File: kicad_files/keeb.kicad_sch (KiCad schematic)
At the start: 169 parts, among them SW1 SW_Push, SW10 SW_Push, SW11 SW_Push, SW12 SW_Push, SW13 SW_Push, SW14 SW_Push, SW15 SW_Push, SW16 SW_Push, SW17 SW_Push, SW18 SW_Push, SW19 SW_Push, SW2 SW_Push, SW20 SW_Push, SW21 SW_Push, SW22 SW_Push, SW23 SW_Push, SW24 SW_Push, SW25 SW_Push, SW26 SW_Push, SW27 SW_Push, SW28 SW_Push, SW29 SW_Push, SW3 SW_Push, SW30 SW_Push, SW31 SW_Push, SW32 SW_Push, SW33 SW_Push, SW34 SW_Push, SW35 SW_Push, SW36 SW_Push, SW37 SW_Push, SW38 SW_Push, SW39 SW_Push, SW4 SW_Push, SW40 SW_Push, SW41 SW_Push, SW42 SW_Push, SW43 SW_Push, SW44 SW_Push, SW45 SW_Push, SW46 SW_Push, SW47 SW_Push, SW48 SW_Push, SW49 SW_Push, SW5 SW_Push, SW50 SW_Push, SW51 SW_Push, SW52 SW_Push, SW53 SW_Push, SW54 SW_Push, SW55 SW_Push, SW56 SW_Push, SW57 SW_Push, SW58 SW_Push, SW59 SW_Push, SW6 SW_Push, SW60 SW_Push, SW61 SW_Push, SW62 SW_Push, SW63 SW_Push, SW64 SW_Push, SW65 SW_Push, SW66 SW_Push, SW67 SW_Push, SW68 SW_Push, SW69 SW_Push, SW7 SW_Push, SW70 SW_Push, SW71 SW_Push, SW72 SW_Push, SW73 SW_Push, SW74 SW_Push, SW75 SW_Push, SW76 SW_Push, SW77 SW_Push, SW78 SW_Push, SW79 SW_Push, SW8 SW_Push, SW80 SW_Push, SW81 SW_Push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

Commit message: Added rgb, better organized schematic
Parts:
- removed D1, D10, D11, D12, D13, D14, D15, D16, D17, D18, D19, D2, D20, D21, D22, D23, D24, D25, D26, D27, D28, D29, D3, D30, D31, D32, D33, D34, D35, D36, D37, D38, D39, D4, D40, D41, D42, D43, D44, D45, D46, D47, D48, D49, D5, D50, D51, D52, D53, D54, D55, D56, D57, D58, D59, D6, D60, D61, D62, D63, D64, D65, D66, D67, D68, D69, D7, D70, D71, D72, D73, D74, D75, D76, D77, D78, D79, D8, D80, D81, D82, D83, D9: 1N4148, digikey-footprints:Diode_DO-35_P10mm, symbol dk_Diodes-Rectifiers-Single:1N4148
- removed S1: MX_stab, PCM_marbastlib-mx:STAB_MX_P_6.25u, symbol PCM_marbastlib-mx:MX_stab
- removed SW1, SW10, SW11, SW12, SW13, SW14, SW15, SW16, SW17, SW18, SW19, SW2, SW20, SW21, SW22, SW23, SW24, SW25, SW26, SW27, SW28, SW29, SW3, SW30, SW31, SW32, SW33, SW34, SW35, SW36, SW37, SW38, SW39, SW4, SW40, SW41, SW42, SW43, SW44, SW45, SW46, SW47, SW48, SW49, SW5, SW50, SW51, SW52, SW53, SW54, SW55, SW56, SW57, SW58, SW59, SW6, SW60, SW61, SW62, SW63, SW64, SW65, SW66, SW67, SW68, SW69, SW7, SW70, SW71, SW72, SW73, SW74, SW75, SW76, SW77, SW78, SW79, SW8, SW80, SW81, SW82, SW83, SW9: SW_Push, symbol Switch:SW_Push
- removed SW84: RotaryEncoder_Switch, symbol Device:RotaryEncoder_Switch
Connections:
- net COL_0: now also A1.1 (GPIO0)
- net COL_1: now also A1.2 (GPIO1)
- net COL_10: now also A1.22 (GPIO17)
- net COL_11: now also A1.21 (GPIO16)
- net COL_2: now also A1.4 (GPIO2)
- net COL_3: now also A1.5 (GPIO3)
- net COL_4: now also A1.6 (GPIO4)
- net COL_5: now also A1.7 (GPIO5)
- net COL_6: now also A1.9 (GPIO6)
- net COL_7: now also A1.10 (GPIO7)
- net COL_8: now also A1.11 (GPIO8)
- net COL_9: now also A1.12 (GPIO9)
- net ROW_0: now also A1.14 (GPIO10)
- net ROW_1: now also A1.15 (GPIO11)
- net ROW_2: now also A1.16 (GPIO12)
- net ROW_3: now also A1.17 (GPIO13)
- net ROW_4: now also A1.19 (GPIO14)
- net GND: now reaches A1.13 (GND), A1.18 (GND), A1.23 (GND), A1.28 (GND), A1.3 (GND), A1.38 (GND), A1.8 (GND)
- net ROT_A: now reaches A1.20 (GPIO15)
- net ROT_B: now reaches A1.24 (GPIO18)
- net LED_DATA: now reaches A1.25 (GPIO19)
- net +5V: now reaches A1.40 (VBUS)
- no-connect marks 0 -> 12
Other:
- added sheet KEY_MATRIX (key_matrix.kicad_sch)
- added sheet LED_MATRIX_LEFT (led_matrix_left.kicad_sch)
- added sheet LED_MATRIX_RIGHT (led_matrix.kicad_sch)
- moved on the sheet: A1

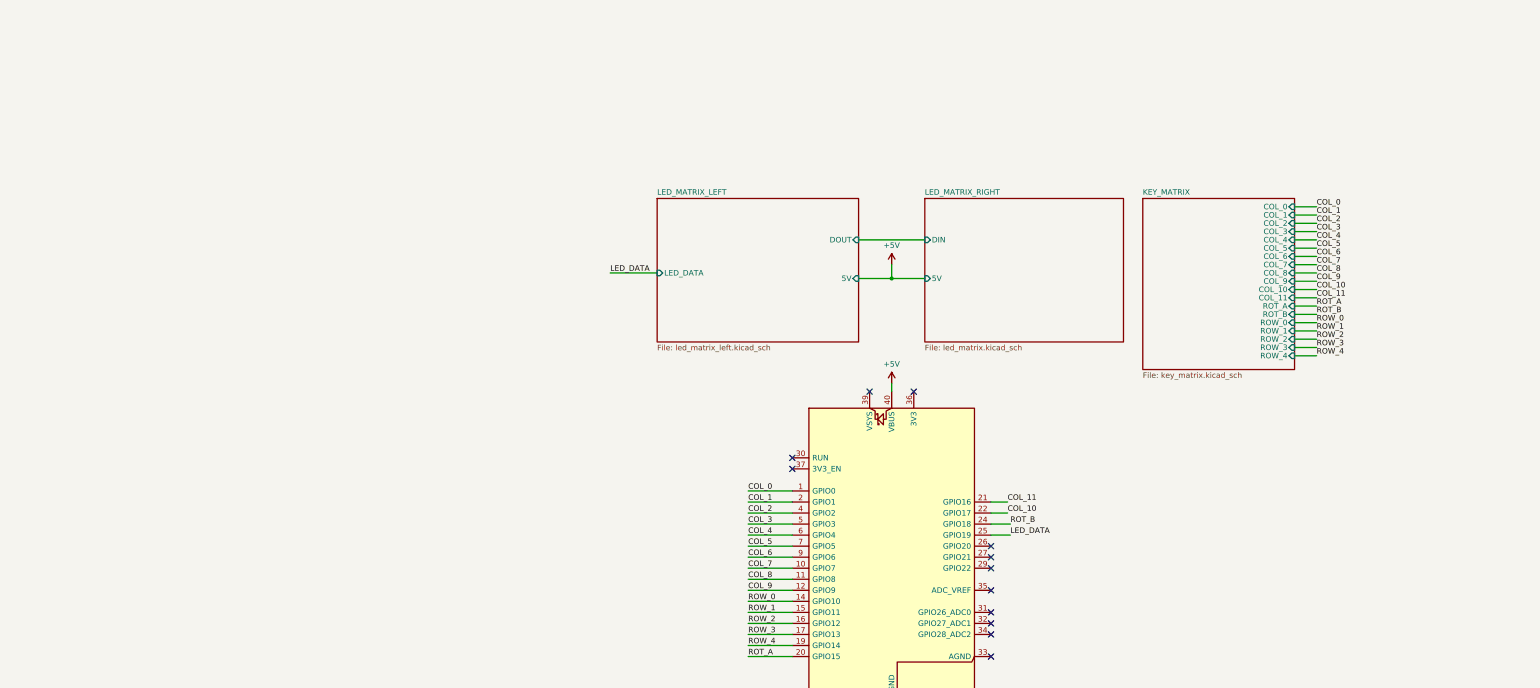
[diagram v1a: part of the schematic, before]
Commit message: Added an oled, 2 stabilisers and 8 mounting holes
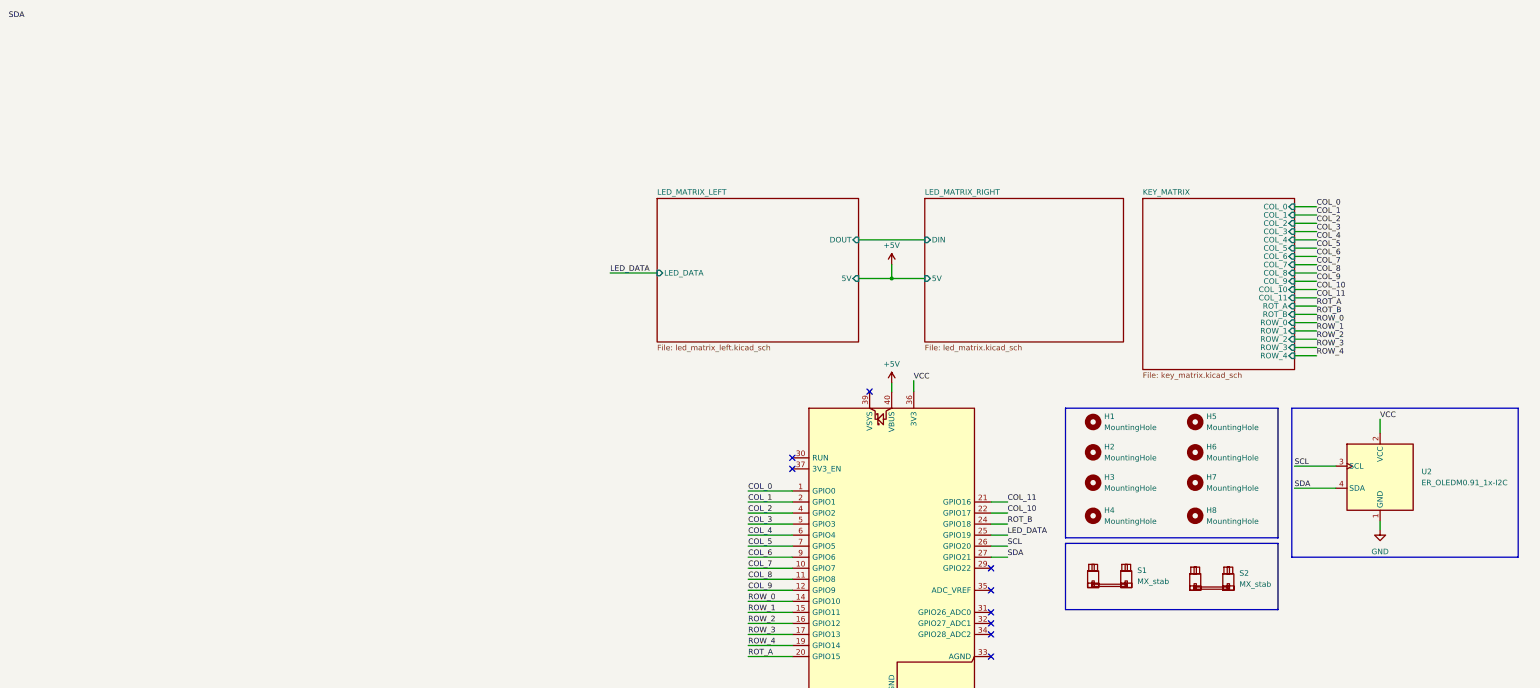
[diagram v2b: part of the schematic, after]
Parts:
- added H1, H2, H3, H4, H5, H6, H7, H8: MountingHole, symbol Mechanical:MountingHole
- added S1, S2: MX_stab, PCM_marbastlib-mx:STAB_MX_P_6.25u, symbol PCM_marbastlib-mx:MX_stab
- added U2: ER_OLEDM0.91_1x-I2C, Display:ER_OLEDM0.91_1x-I2C, symbol Display_Graphic:ER_OLEDM0.91_1x-I2C
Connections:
- net GND: now also U2.1 (GND)
- net SCL: now reaches A1.26 (GPIO20)
- net SCL: now also U2.3 (SCL)
- net SDA: now reaches A1.27 (GPIO21)
- net SDA: now also U2.4 (SDA)
- net VCC: now reaches A1.36 (3V3)
- net VCC: now also U2.2 (VCC)
- no-connect marks 12 -> 9
